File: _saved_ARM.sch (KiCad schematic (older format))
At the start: 18 parts, among them SW601 SW_DIP_x01, SW602 SW_DPDT_x2, U601 STM32F303CCT6, Y601 32.768kHz, Y602 8MHz

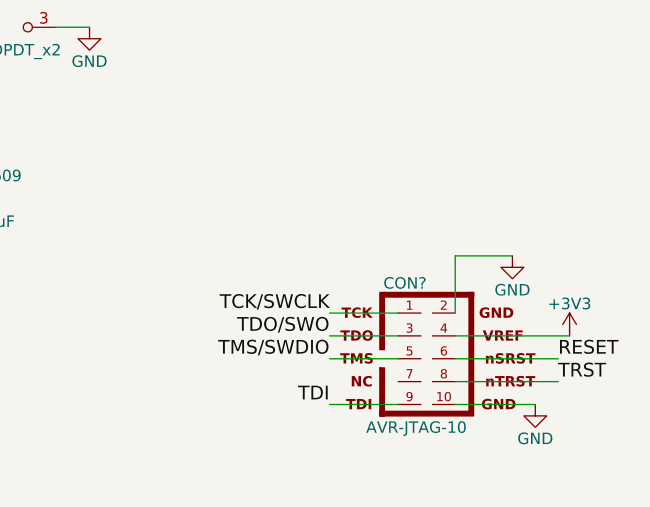
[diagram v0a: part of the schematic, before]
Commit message: Started associating footprints
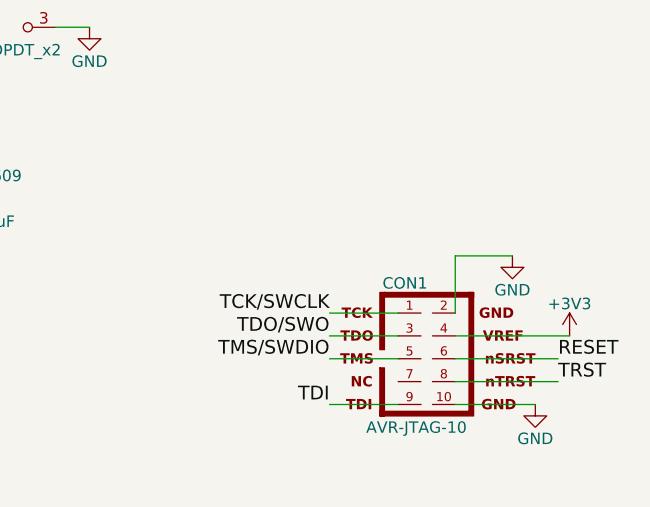
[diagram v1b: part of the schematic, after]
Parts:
- CON1: renamed from CON?; footprint AVR-JTAG-10 -> Pin_Headers:Pin_Header_Straight_2x05_Pitch2.54mm
- R601, R602, R603: footprint (none) -> Resistors_SMD:R_0402
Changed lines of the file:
@@
 F 0 "R602" V 2130 3000 50  0000 C CNN
 F 1 "390" V 2050 3000 50  0000 C CNN
-F 2 "" V 1980 3000 50  0001 C CNN
+F 2 "Resistors_SMD:R_0402" V 1980 3000 50  0001 C CNN
 F 3 "" H 2050 3000 50  0001 C CNN
 	1    2050 3000
@@
 F 0 "R603" V 6530 2900 50  0000 C CNN
 F 1 "10k" V 6450 2900 50  0000 C CNN
-F 2 "" V 6380 2900 50  0001 C CNN
+F 2 "Resistors_SMD:R_0402" V 6380 2900 50  0001 C CNN
 F 3 "" H 6450 2900 50  0001 C CNN
 	1    6450 2900
@@
 F 0 "R601" V 2130 2500 50  0000 C CNN
 F 1 "0" V 2050 2500 50  0000 C CNN
-F 2 "" V 1980 2500 50  0001 C CNN
+F 2 "Resistors_SMD:R_0402" V 1980 2500 50  0001 C CNN
 F 3 "" H 2050 2500 50  0001 C CNN
 	1    2050 2500
@@
 $EndComp
 $Comp
-L AVR-JTAG-10 CON?
+L AVR-JTAG-10 CON1
 U 1 1 5ACC0630
 P 8700 4450
-F 0 "CON?" H 8530 4780 50  0000 C CNN
+F 0 "CON1" H 8530 4780 50  0000 C CNN
 F 1 "AVR-JTAG-10" H 8360 4120 50  0000 L BNN
-F 2 "AVR-JTAG-10" V 8130 4470 50  0001 C CNN
+F 2 "Pin_Headers:Pin_Header_Straight_2x05_Pitch2.54mm" V 8130 4470 50  0001 C CNN
 F 3 "" H 8700 4450 50  0001 C CNN
 	1    8700 4450
@@
 RESET
 $Comp
-L +3V3 #PWR?
+L +3V3 #PWR048
 U 1 1 5ACC11E3
 P 9250 4350
-F 0 "#PWR?" H 9250 4200 50  0001 C CNN
+F 0 "#PWR048" H 9250 4200 50  0001 C CNN
 F 1 "+3V3" H 9250 4490 50  0000 C CNN
 F 2 "" H 9250 4350 50  0001 C CNN
@@
 $EndComp
 $Comp
-L GND #PWR?
+L GND #PWR049
 U 1 1 5ACC1230
 P 9000 4000
-F 0 "#PWR?" H 9000 3750 50  0001 C CNN
+F 0 "#PWR049" H 9000 3750 50  0001 C CNN
 F 1 "GND" H 9000 3850 50  0000 C CNN
 F 2 "" H 9000 4000 50  0001 C CNN
@@
 	8750 4000 9000 4000
 $Comp
-L GND #PWR?
+L GND #PWR050
 U 1 1 5ACC189B
 P 9100 4650
-F 0 "#PWR?" H 9100 4400 50  0001 C CNN
+F 0 "#PWR050" H 9100 4400 50  0001 C CNN
 F 1 "GND" H 9100 4500 50  0000 C CNN
 F 2 "" H 9100 4650 50  0001 C CNN
